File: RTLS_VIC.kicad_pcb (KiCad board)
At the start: 2 copper layers, 70 x 70 mm, 57 parts, among them J1 Conn_01x07_Socket, J10 Conn_01x04_Socket, J11 Conn_01x04_Socket, J12 Conn_01x02_Pin, J13 Conn_01x04_Socket, J14 Conn_01x03_Pin, J15 Conn_01x03_Pin, J16 Conn_01x03_Pin, J17 Conn_01x03_Pin, J3 Conn_01x03_Pin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

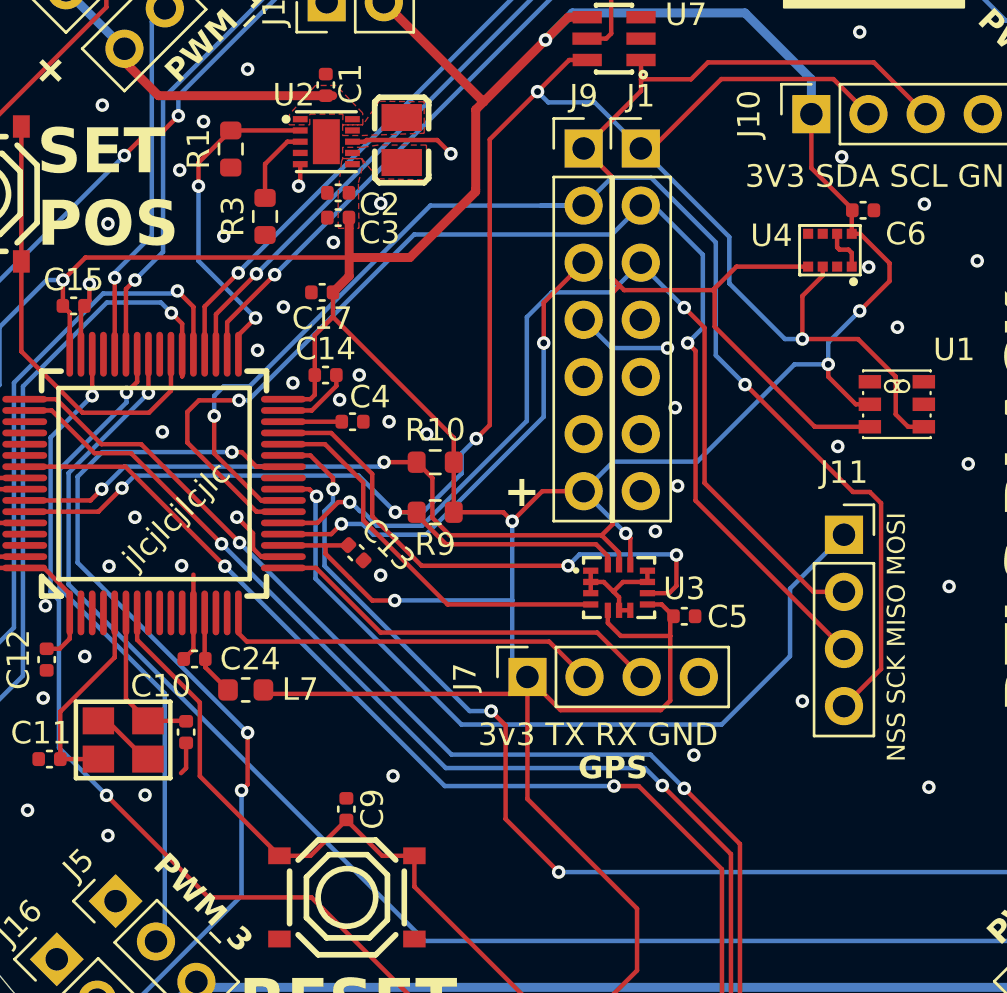
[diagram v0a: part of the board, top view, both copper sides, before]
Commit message: fix issues with power supply
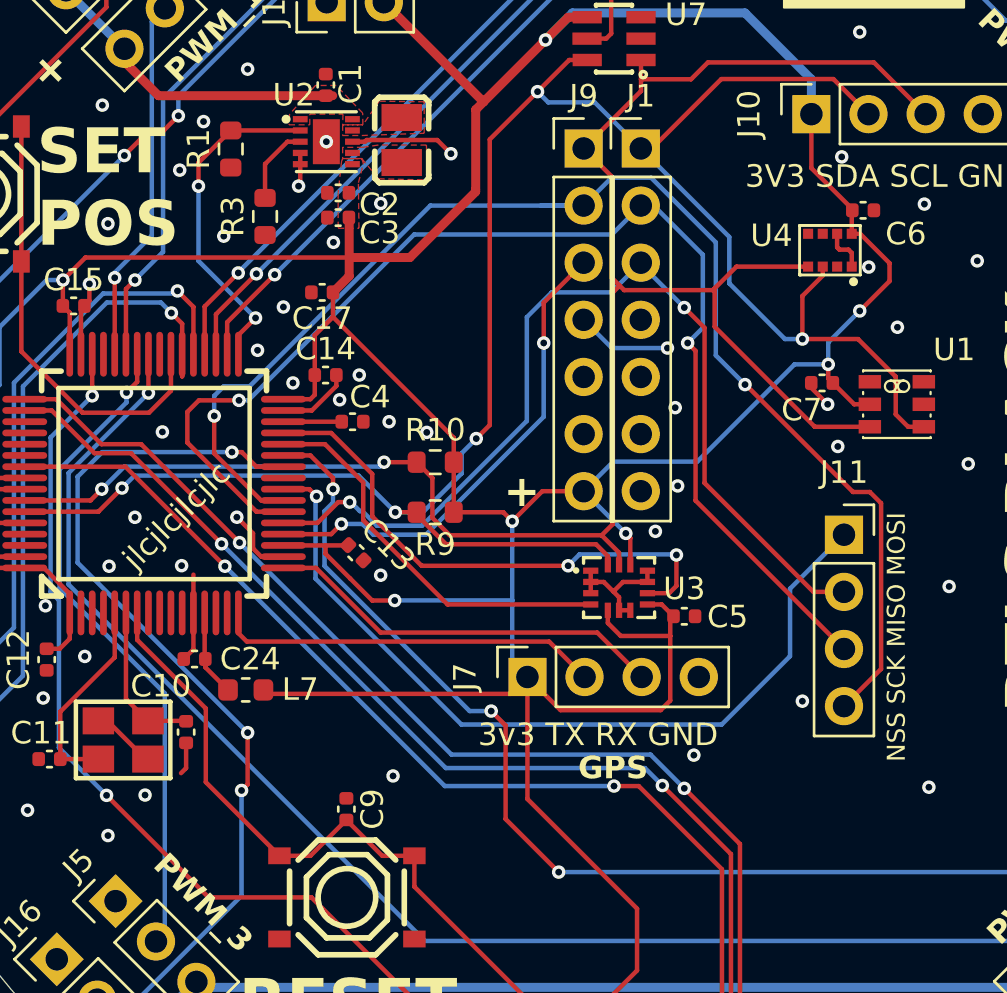
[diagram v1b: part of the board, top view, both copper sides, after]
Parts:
- added C7: 100nF, Capacitor_SMD:C_0402_1005Metric, F.Cu at (165.2, 88.4)
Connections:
- U2 pad 11: unconnected-(U2-EP-Pad11) -> GND
- U2 pad 4: unconnected-(U2-CFG2-Pad4) -> GND
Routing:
- net GND: track 40.9 -> 42.7 mm, vias 79 -> 81
